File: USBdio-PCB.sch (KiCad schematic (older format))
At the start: 68 parts, among them IC1 ATMEGA328-P, P0 TE_RELAY_(ORWH-SH-112D), P1 TE_RELAY_(ORWH-SH-112D), P2 TE_RELAY_(ORWH-SH-112D), P3 TE_RELAY_(ORWH-SH-112D), P4 TE_RELAY_(ORWH-SH-112D), P5 TE_RELAY_(ORWH-SH-112D), P6 TE_RELAY_(ORWH-SH-112D), P7 TE_RELAY_(ORWH-SH-112D), Q1 Q_NPN_BEC, Q10 Q_NPN, Q11 Q_NPN, Q12 Q_NPN, Q13 Q_NPN, Q14 Q_NPN, Q15 Q_NPN, Q16 Q_NPN, Q17 Q_NPN, Q2 Q_NPN_BEC, Q3 Q_NPN_BEC, Q4 Q_NPN_BEC, Q5 Q_NPN_BEC, Q6 Q_NPN_BEC, Q7 Q_NPN_BEC, Q8 Q_NPN_BEC, Q9 Q_NPN_BEC

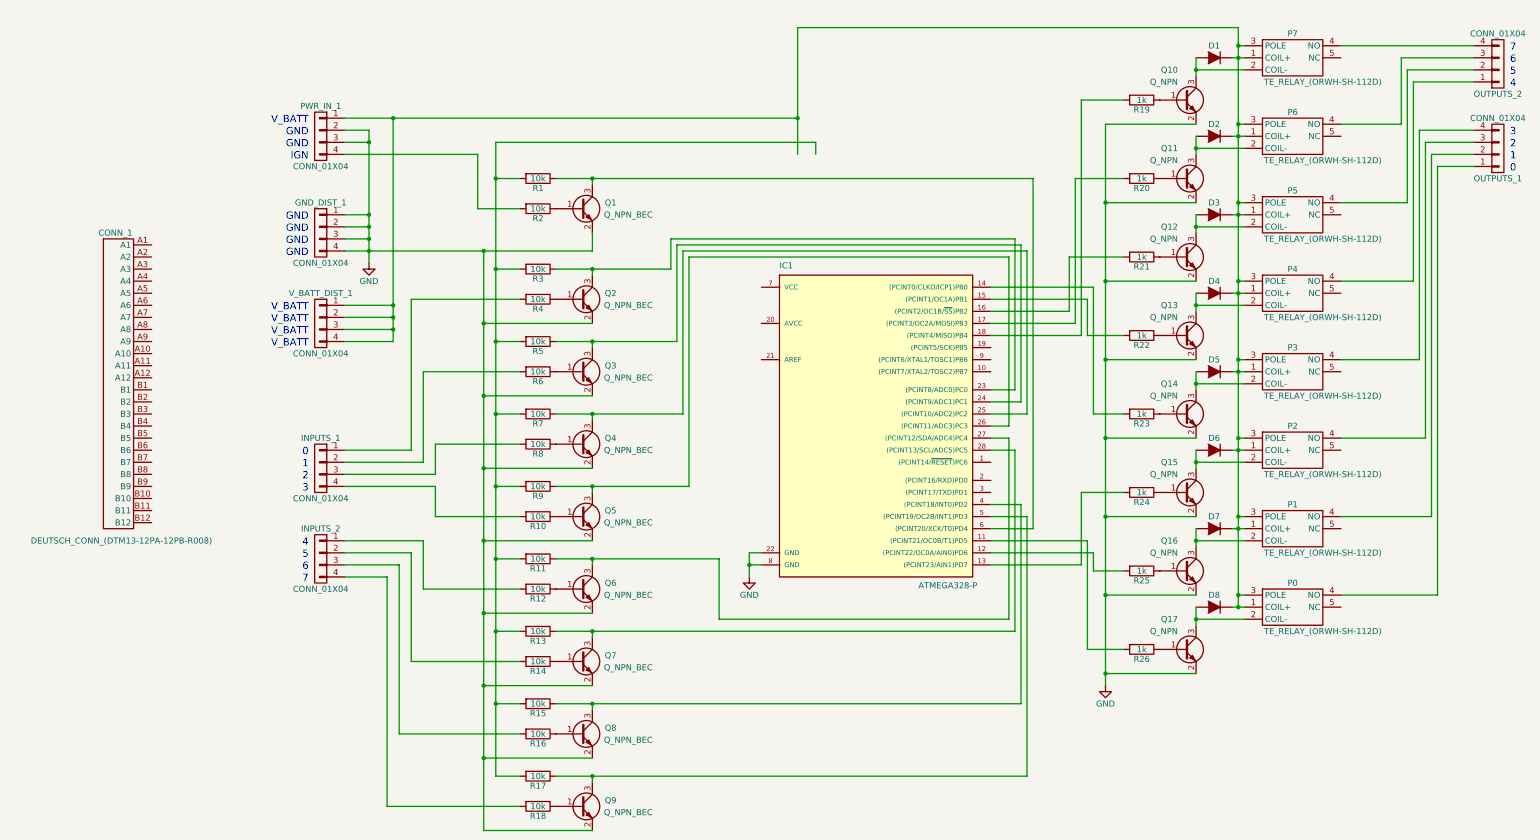
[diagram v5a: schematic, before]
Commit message: all footprints added.  ready for traces.
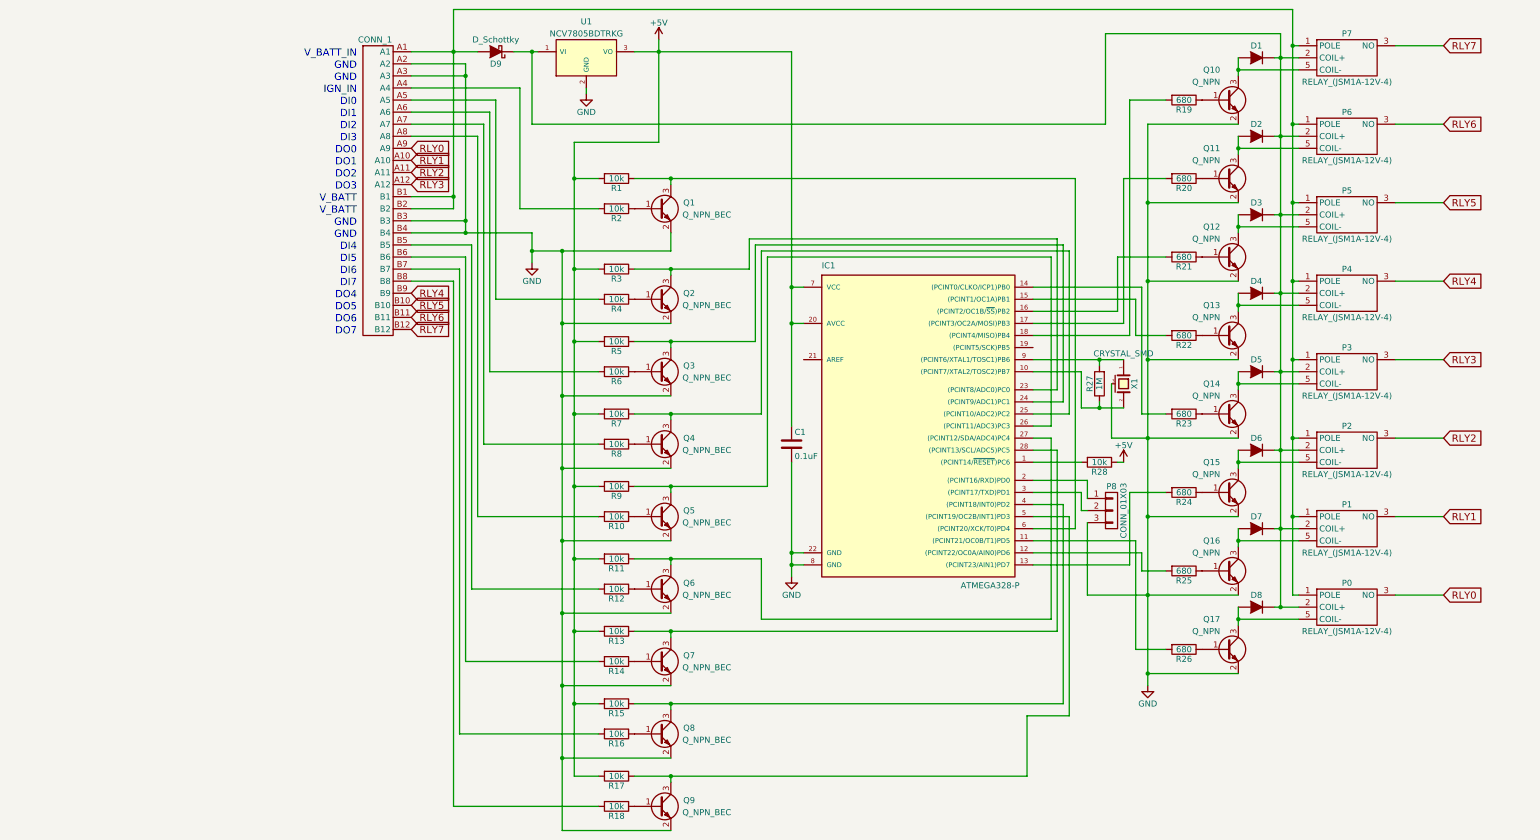
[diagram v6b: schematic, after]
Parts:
- removed GND_DIST_1, INPUTS_1, INPUTS_2, OUTPUTS_1, OUTPUTS_2, PWR_IN_1, V_BATT_DIST_1: CONN_01X04, USBdio-PCB:PHX_HDR_4_POS_(1933202), symbol CONN_01X04
- removed P0, P1, P2, P3, P4, P5, P6, P7: TE_RELAY_(ORWH-SH-112D), USBdio-PCB:TE_RELAY_(ORWH-SH-112D), symbol TE_RELAY_(ORWH-SH-112D)
- added C1: 0.1uF, symbol C
- added D9: D_Schottky, USBdio-PCB:SCHOTTKY_(PMEG3030EP,115), symbol D_Schottky
- added P0, P1, P2, P3, P4, P5, P6, P7: RELAY_(JSM1A-12V-4), symbol RELAY_(JSM1A-12V-4)
- added P8: CONN_01X03, Pin_Headers:Pin_Header_Straight_1x03, symbol CONN_01X03
- added R27: 1M, Resistors_SMD:R_1206_HandSoldering, symbol R
- added R28: 10k, Resistors_SMD:R_1206_HandSoldering, symbol R
- added U1: NCV7805BDTRKG, USBdio-PCB:REGULATOR_(NCV7805BDTRKG), symbol NCV7805BDTRKG
- added X1: CRYSTAL_SMD, USBdio-PCB:RESONATOR_(CSTCE16M0V53C-R0), symbol CRYSTAL_SMD
- R19, R20, R21, R22, R23, R24, R25, R26: value 1k -> 680
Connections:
- net GND: now also CONN_1.A2, CONN_1.A3, CONN_1.B3, CONN_1.B4, C1.2, P8.3 (P3), U1.2 (GND), X1.3 (case)
- net at D1.1 (K), D2.1 (K), D3.1 (K)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: now also D9.1 (K), P0.2 (COIL+), P1.2 (COIL+), P2.2 (COIL+), P3.2 (COIL+), P4.2 (COIL+), P5.2 (COIL+), P6.2 (COIL+), P7.2 (COIL+), U1.1 (VI)
- net at R2.2: now also CONN_1.A4
- net at R4.2: now also CONN_1.A5
- net +5V: now reaches R1.2, R11.2, R13.2, R15.2, R17.2, R3.2, R5.2, R7.2, R9.2
- net +5V: now also IC1.20 (AVCC), IC1.7 (VCC), C1.1, R28.1, U1.3 (VO)
- net at R6.2: now also CONN_1.A6
- net at R8.2: now also CONN_1.A7
- net at R10.2: now also CONN_1.A8
- net at R12.2: now also CONN_1.B5
- net at R14.2: now also CONN_1.B6
- net at R16.2: now also CONN_1.B7
- net at R18.2: now also CONN_1.B8
- net at D1.2 (A), Q10.3 (C): now also P7.5 (COIL-)
- net at D2.2 (A), Q11.3 (C): now also P6.5 (COIL-)
- net at D3.2 (A), Q12.3 (C): now also P5.5 (COIL-)
- net at D4.2 (A), Q13.3 (C): now also P4.5 (COIL-)
- net at D5.2 (A), Q14.3 (C): now also P3.5 (COIL-)
- net at D6.2 (A), Q15.3 (C): now also P2.5 (COIL-)
- net at D7.2 (A), Q16.3 (C): now also P1.5 (COIL-)
- net at D8.2 (A), Q17.3 (C): now also P0.5 (COIL-)
- net at CONN_1.A1: now also CONN_1.B1, CONN_1.B2, D9.2 (A), P0.1 (POLE), P1.1 (POLE), P2.1 (POLE), P3.1 (POLE), P4.1 (POLE), P5.1 (POLE), P6.1 (POLE), P7.1 (POLE)
- net RLY1: now reaches CONN_1.A10
- net RLY1: now also P1.3 (NO)
- net RLY2: now reaches CONN_1.A11
- net RLY2: now also P2.3 (NO)
- net RLY3: now reaches CONN_1.A12
- net RLY3: now also P3.3 (NO)
- net RLY0: now reaches CONN_1.A9
- net RLY0: now also P0.3 (NO)
- net RLY5: now reaches CONN_1.B10
- net RLY5: now also P5.3 (NO)
- net RLY6: now reaches CONN_1.B11
- net RLY6: now also P6.3 (NO)
- net RLY7: now reaches CONN_1.B12
- net RLY7: now also P7.3 (NO)
- net RLY4: now reaches CONN_1.B9
- net RLY4: now also P4.3 (NO)
- net at IC1.1 ((PCINT14/~RESET~)PC6): now also R28.2
- net at IC1.10 ((PCINT7/XTAL2/TOSC2)PB7): now also R27.1, X1.2
- net at IC1.2 ((PCINT16/RXD)PD0): now also P8.1 (P1)
- net at IC1.3 ((PCINT17/TXD)PD1): now also P8.2 (P2)
- net at IC1.9 ((PCINT6/XTAL1/TOSC1)PB6): now also R27.2, X1.1
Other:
- note added: "DI0"
- note added: "DI1"
- note added: "DI2"
- note added: "DI3"
- note added: "DI4"
- note added: "DI5"
- note added: "DI6"
- note added: "DI7"
- note added: "DO0"
- note added: "DO1"
- note added: "DO2"
- note added: "DO3"
- note added: "DO4"
- note added: "DO5"
- note added: "DO6"
- note added: "DO7"
- note added: "IGN_IN"
- note added: "V_BATT_IN"
- note removed: "0"
- note removed: "1"
- note removed: "2"
- note removed: "3"
- note removed: "4"
- note removed: "5"
- note removed: "6"
- note removed: "7"
- note removed: "IGN"
- moved on the sheet: CONN_1, D1, D2, D3, D4, D5, D6, D7, D8, IC1, Q1, Q10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

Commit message: almost finish with traces.
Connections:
- net GND: no longer CONN_1.A2, CONN_1.A3, CONN_1.B3, CONN_1.B4
- net RLY4: now also CONN_1.B1; no longer CONN_1.B9
- net RLY5: now also CONN_1.B2; no longer CONN_1.B10
- net RLY6: now also CONN_1.B3; no longer CONN_1.B11
- net RLY7: now also CONN_1.B4; no longer CONN_1.B12
- net at CONN_1.A1, D9.2 (A), P0.1 (POLE)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: now also CONN_1.B10, CONN_1.B9; no longer CONN_1.B1, CONN_1.B2
- new net: CONN_1.A2, CONN_1.A3, CONN_1.B11, CONN_1.B12
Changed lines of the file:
@@
 Text Notes 1300 2900 2    60   ~ 0
 DI7
+Text Notes 1300 2200 2    60   ~ 0
+DO4
+Text Notes 1300 2300 2    60   ~ 0
+DO5
+Text Notes 1300 2400 2    60   ~ 0
+DO6
+Text Notes 1300 2500 2    60   ~ 0
+DO7
+Text Notes 1300 3300 2    60   ~ 0
+GND
+Text Notes 1300 3200 2    60   ~ 0
+GND
 Text Notes 1300 3000 2    60   ~ 0
-DO4
+V_BATT
 Text Notes 1300 3100 2    60   ~ 0
-DO5
-Text Notes 1300 3200 2    60   ~ 0
-DO6
-Text Notes 1300 3300 2    60   ~ 0
-DO7
-Text Notes 1300 2500 2    60   ~ 0
-GND
-Text Notes 1300 2400 2    60   ~ 0
-GND
-Text Notes 1300 2200 2    60   ~ 0
-V_BATT
-Text Notes 1300 2300 2    60   ~ 0
 V_BATT
 $Comp
@@
 Text GLabel 1750 2050 2    60   Input ~ 0
 RLY3
-Text GLabel 1750 2950 2    60   Input ~ 0
+Text GLabel 1750 2150 2    60   Input ~ 0
 RLY4
-Text GLabel 1750 3050 2    60   Input ~ 0
+Text GLabel 1750 2250 2    60   Input ~ 0
 RLY5
-Text GLabel 1750 3150 2    60   Input ~ 0
+Text GLabel 1750 2350 2    60   Input ~ 0
 RLY6
-Text GLabel 1750 3250 2    60   Input ~ 0
+Text GLabel 1750 2450 2    60   Input ~ 0
 RLY7
 Wire Wire Line
@@
 Connection ~ 3100 6350
 Wire Wire Line
-	2250 5400 3300 5400
-Wire Wire Line
-	2200 6000 3300 6000
-Wire Wire Line
-	2150 6600 3300 6600
-Wire Wire Line
-	2100 7200 3300 7200
+	2050 5400 3300 5400
+Wire Wire Line
+	2000 6000 3300 6000
+Wire Wire Line
+	1950 6600 3300 6600
+Wire Wire Line
+	1900 7200 3300 7200
 Wire Wire Line
 	3900 2600 3900 2450
@@
 	9050 600  2100 600
 Wire Wire Line
-	2100 600  2100 2250
+	2100 600  2100 2950
 Connection ~ 2100 950
 Wire Wire Line
@@
 	2300 4800 3300 4800
 Wire Wire Line
-	1750 2550 2250 2550
-Wire Wire Line
-	2250 2550 2250 5400
-Wire Wire Line
-	2200 6000 2200 2650
-Wire Wire Line
-	2200 2650 1750 2650
-Wire Wire Line
-	1750 2750 2150 2750
-Wire Wire Line
-	2150 2750 2150 6600
-Wire Wire Line
-	2100 7200 2100 2850
-Wire Wire Line
-	2100 2850 1750 2850
+	1750 2550 2050 2550
+Wire Wire Line
+	2050 2550 2050 5400
+Wire Wire Line
+	2000 6000 2000 2650
+Wire Wire Line
+	2000 2650 1750 2650
+Wire Wire Line
+	1750 2750 1950 2750
+Wire Wire Line
+	1950 2750 1950 6600
+Wire Wire Line
+	1900 7200 1900 2850
+Wire Wire Line
+	1900 2850 1750 2850
 Wire Wire Line
 	2750 2450 2750 2700
-Wire Wire Line
-	1750 2450 2750 2450
 Connection ~ 2750 2600
 Wire Wire Line
 	1750 1050 2200 1050
 Wire Wire Line
-	2200 1050 2200 2450
-Connection ~ 2200 2450
-Wire Wire Line
-	1750 2350 2200 2350
-Connection ~ 2200 2350
+	2200 1050 2200 3150
 Wire Wire Line
 	1750 1150 2200 1150
@@
 	2750 1550 2750 950
 Connection ~ 2750 950
-Wire Wire Line
-	2100 2250 1750 2250
-Wire Wire Line
-	1750 2150 2100 2150
-Connection ~ 2100 2150
 $Comp
 L RELAY_(JSM1A-12V-4) P7
@@
 Wire Wire Line
 	7350 5450 7350 4850
+Wire Wire Line
+	2100 2950 1750 2950
+Wire Wire Line
+	1750 3050 1800 3050
+Wire Wire Line
+	1800 3050 1800 2950
+Connection ~ 1800 2950
+Wire Wire Line
+	2200 3150 1750 3150
+Wire Wire Line
+	1750 3250 1800 3250
+Wire Wire Line
+	1800 3250 1800 3150
+Connection ~ 1800 3150
 $EndSCHEMATC

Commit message: finished traces
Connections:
- net GND: now also CONN_1.A1, CONN_1.A2, CONN_1.B11, CONN_1.B12
- net RLY0: now also CONN_1.A7; no longer CONN_1.A9
- net RLY1: now also CONN_1.A8; no longer CONN_1.A10
- net RLY2: now also CONN_1.A9; no longer CONN_1.A11
- net RLY3: now also CONN_1.A10; no longer CONN_1.A12
- net RLY4: now also CONN_1.B3; no longer CONN_1.B1
- net RLY5: now also CONN_1.B4; no longer CONN_1.B2
- net RLY6: now also CONN_1.B5; no longer CONN_1.B3
- net RLY7: now also CONN_1.B6; no longer CONN_1.B4
- net at R4.2: now also CONN_1.A3; no longer CONN_1.A5
- net at R6.2: now also CONN_1.A4; no longer CONN_1.A6
- net at R8.2: now also CONN_1.A5; no longer CONN_1.A7
- net at R10.2: now also CONN_1.A6; no longer CONN_1.A8
- net at R12.2: now also CONN_1.B7; no longer CONN_1.B5
- net at R14.2: now also CONN_1.B8; no longer CONN_1.B6
- net at R16.2: now also CONN_1.B9; no longer CONN_1.B7
- net at R18.2: now also CONN_1.B10; no longer CONN_1.B8
- net at R2.2: now also CONN_1.A11; no longer CONN_1.A4
- net at D9.2 (A), P0.1 (POLE), P1.1 (POLE)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: now also CONN_1.A12, CONN_1.B1, CONN_1.B2; no longer CONN_1.A1, CONN_1.B10, CONN_1.B9
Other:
- moved on the sheet: CONN_1
